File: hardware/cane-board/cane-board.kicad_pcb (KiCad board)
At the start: 2 copper layers, 40 x 100 mm, 99 parts, among them J1 12V battery, J10 Phone power, J11 Firmware, J2 Motor, J3 Kill switch, J4 Talk button, J5 Encoder, J6 I2C, J7 Buzzer motor, J8 Serial, Q1 AO3401A, Q2 AO3401A, Q3 AO3400A, Q4 AO3401A, SW1 Reset, SW2 Boot, SW3 Power, U1 ESP32-S3-WROOM-1-N4, U2 DRV8876PWPR, U3 TPS54302DDCR, U4 AP2112K-3.3, U5 TPS2069CDBVR

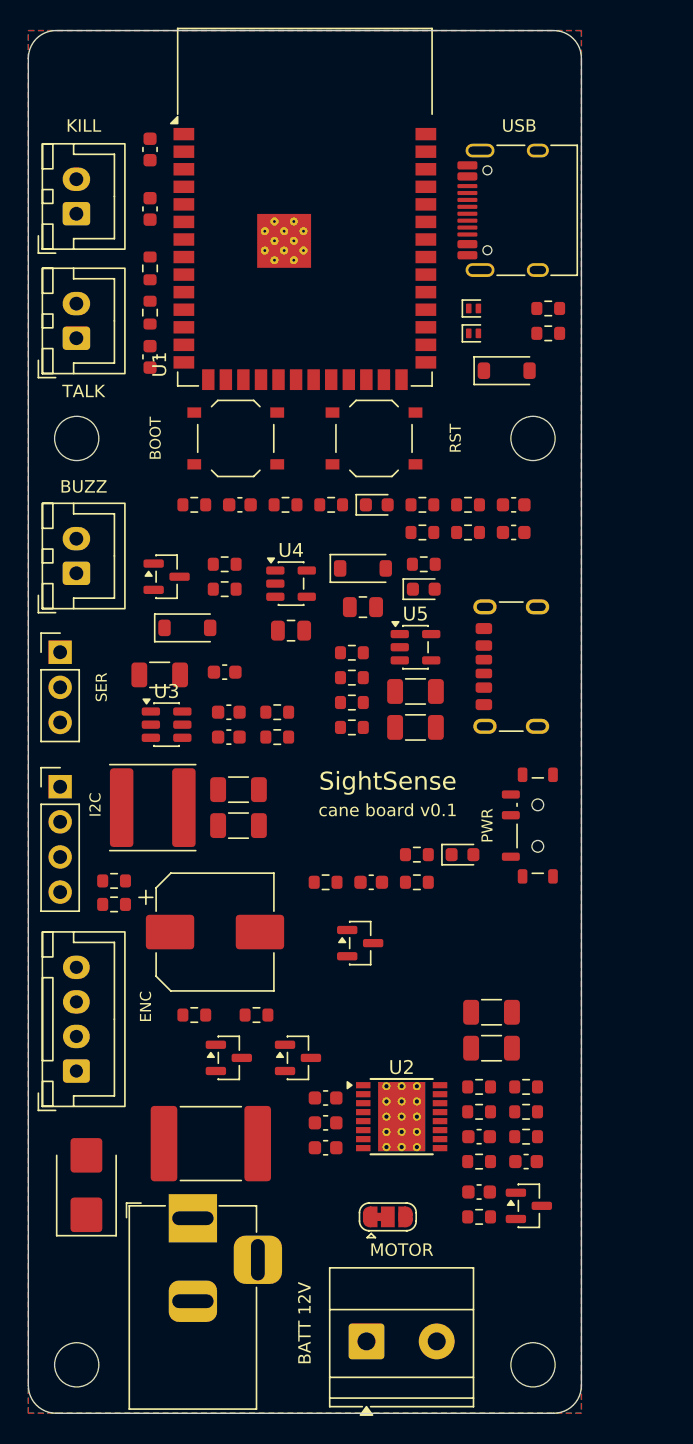
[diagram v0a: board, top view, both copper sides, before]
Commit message: Route the cane board on 4 layers with black mask
make_route.py hands the placed board to Freerouting, widens the motor
supply, pours ground on every layer and stitches it, then runs KiCad's
design rules check: 0 errors, 0 unconnected, matches the schematic.
Adds board rules, mounting screws to the BOM and the 4-layer price.
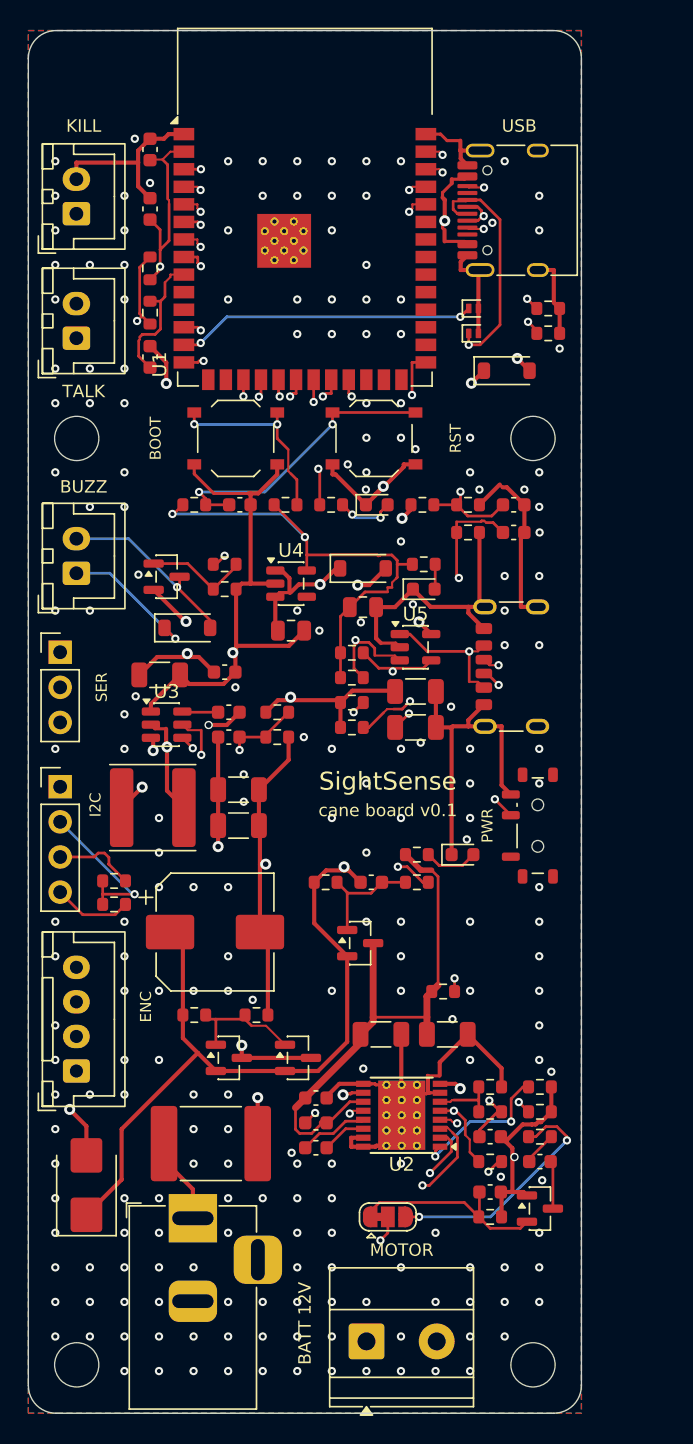
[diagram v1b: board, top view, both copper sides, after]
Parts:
- moved R26 33.2 mm to (30.0, 69.5)
- moved C3 8.16 mm to (25.5, 72.6)
- moved C27 3.35 mm to (30.3, 72.6)
- moved C8 1.00 mm to (37.0, 81.8)
- moved R10 1.00 mm to (37.0, 80.0)
- moved R8 1.00 mm to (37.0, 76.4)
- moved R9 1.00 mm to (37.0, 78.2)
- moved D4 0.82 mm to (37.0, 85.2)
- moved C7 0.80 mm to (33.4, 80.0)
- moved C9 0.80 mm to (33.4, 84.0)
- moved R11 0.80 mm to (33.4, 85.8)
- moved R5 0.80 mm to (33.4, 76.4)
- moved R6 0.80 mm to (33.4, 78.2)
- moved R7 0.80 mm to (33.4, 81.8)
- moved C4 0.70 mm to (20.8, 77.2)
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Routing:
- net GND: track 0.00 -> 210.3 mm, vias 0 -> 218
- net +3V3: track 0.00 -> 164.7 mm, vias 0 -> 6
- net +BATT: track 0.00 -> 107.5 mm, vias 0 -> 4
- net /MOT_EN: track 0.00 -> 102.7 mm, vias 0 -> 3
- net /HBEAT: track 0.00 -> 95.9 mm, vias 0 -> 3
- net /VM_ADC: track 0.00 -> 92.5 mm, vias 0 -> 4
- net /MOT_PH: track 0.00 -> 89.6 mm, vias 0 -> 3
- net /DRV_FLT: track 0.00 -> 88.6 mm, vias 0 -> 4
- net /I_ADC: track 0.00 -> 75.3 mm, vias 0 -> 2
- net +5V: track 0.00 -> 63.6 mm, vias 0 -> 5
- net /KILL_A: track 0.00 -> 63.3 mm, vias 0 -> 2
- net /UART_RX: track 0.00 -> 61.5 mm, vias 0 -> 1
- net /ENC_B: track 0.00 -> 60.2 mm, vias 0 -> 1
- net /ENC_A: track 0.00 -> 52.3 mm, vias 0 -> 1
- net /SDA: track 0.00 -> 50.6 mm, vias 0 -> 1
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- added copper zone on In1.Cu, net GND
- added copper zone on In2.Cu, net GND
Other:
- copper layers 2 -> 4

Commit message: Reroute the cane board at 46 x 100 mm with power on the outer layers
No copper under the ESP32 aerial on any layer; battery, motor and
converter tracks kept to the outer layers; design rules check 0 errors,
0 unconnected, matches the schematic. Adds make_fab.py and the JLCPCB
ordering files. Parts of the VM and MOT_A tracks are still narrow.
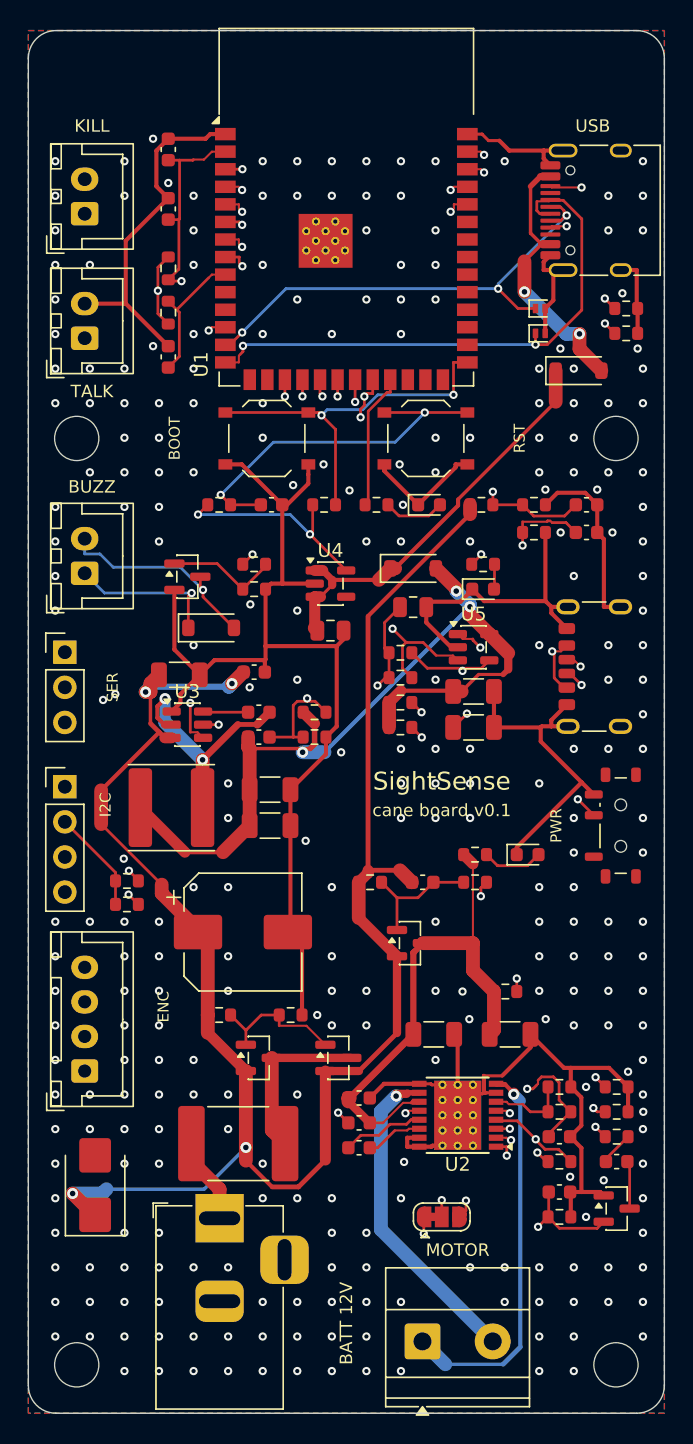
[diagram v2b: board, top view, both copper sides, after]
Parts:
- moved H2 6.00 mm to (42.5, 29.5)
- moved H4 6.00 mm to (42.5, 96.5)
- moved J10 6.00 mm to (42.0, 46.0)
- moved J11 6.00 mm to (41.8, 13.0)
- moved SW3 6.00 mm to (42.8, 57.5)
- moved R19 5.64 mm to (43.2, 20.1)
- moved R20 5.64 mm to (43.2, 21.9)
- moved C8 5.55 mm to (42.5, 81.8)
- moved D4 5.55 mm to (42.5, 85.2)
- moved R10 5.55 mm to (42.5, 80.0)
- moved R8 5.55 mm to (42.5, 76.4)
- moved R9 5.55 mm to (42.5, 78.2)
- moved C22 5.27 mm to (40.4, 34.3)
- moved C23 5.27 mm to (40.4, 36.3)
- moved D6 5.19 mm to (39.8, 24.6)
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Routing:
- net GND: track 210.3 -> 238.4 mm, vias 218 -> 277
- net +BATT: track 107.5 -> 133.3 mm
- net /KILL_A: track 63.3 -> 78.6 mm
- net +3V3: track 164.7 -> 179.4 mm, vias 6 -> 8
- net /UART_RX: track 61.5 -> 50.3 mm
- net /MOT_EN: track 102.7 -> 91.6 mm
- net /BUCK_FB: track 9.93 -> 19.6 mm
- net /VM_ADC: track 92.5 -> 83.6 mm, vias 4 -> 3
- net /ENC_B: track 60.2 -> 52.2 mm, vias 1 -> 3
- net /ENC_A: track 52.3 -> 59.3 mm, vias 1 -> 3
- net /MOT_A: track 23.1 -> 28.4 mm
- net /ESP_EN: track 46.6 -> 51.9 mm
- net /BUCK_SW: track 13.7 -> 18.1 mm
- net /PH_CC1: track 14.3 -> 18.6 mm
- net /DRV_FLT: track 88.6 -> 84.4 mm, vias 4 -> 2
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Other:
- board size 40 x 100 mm -> 46 x 100 mm

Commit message: Cane board: 5 V module, XT30 motor socket, 2.2 A limit, hand-routed power
Replace the TPS54302 converter with a sealed K7805-1000R3 module and
move the power switch to the 3.3 V regulator's enable. Swap the motor
screw terminal for an upright XT30. Raise the current limit to 2.2 A
(R5 1.5k) to match the push the IBT-2 gave.

Draw the battery, motor-supply and motor tracks by hand (0.6-1.0 mm on
the outer layers) before autorouting, turn J2 and C4 round so those
tracks run straight, and tie stranded ground pads to a via. DRC: 0
errors, 0 unconnected. Update the BOM, cost, problems list and fab files.
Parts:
- removed C12: 100nF 50V, Capacitor_SMD:C_0603_1608Metric
- removed C25: 100pF, Capacitor_SMD:C_0603_1608Metric
- removed L1: 10uH 3.2A, Inductor_SMD:L_Changjiang_FNR6045S
- removed R13: 13k, Resistor_SMD:R_0603_1608Metric
- J2: footprint TerminalBlock_Phoenix:TerminalBlock_Phoenix_MKDS-1,5-2-5.08_1x02_P5.08mm_Horizontal -> Connector_AMASS:AMASS_XT30UPB-F_1x02_P5.0mm_Vertical
- R5: value 2.2k -> 1.5k
- U3: value TPS54302DDCR -> K7805-1000R3; footprint Package_TO_SOT_SMD:SOT-23-6 -> Converter_DCDC:Converter_DCDC_RECOM_R-78E-0.5_THT
- moved C13 5.12 mm to (22.6, 54.9)
- moved C14 5.12 mm to (22.6, 57.5)
- moved J2 5.05 mm to (33.5, 94.5), turned to 180 degrees
- moved U3 4.66 mm to (10.5, 54.8)
- moved R12 1.70 mm to (20.7, 47.6)
- turned C4 to 180 degrees
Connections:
- R12 pad 1: +5V -> /VSYS
- R12 pad 2: /BUCK_FB -> /LDO_EN
- SW3 pad 2: /BUCK_EN -> /LDO_EN
- U3 pad 1: GND -> +BATT
- U3 pad 2: /BUCK_SW -> GND
- U3 pad 3: +BATT -> +5V
- U4 pad 3: /VSYS -> /LDO_EN
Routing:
- net /LDO_EN: track 0.00 -> 37.8 mm, vias 0 -> 2
- net /BUCK_EN: track 31.0 -> 0.00 mm, vias 2 -> 0
- net GND: track 238.4 -> 209.5 mm, vias 277 -> 263
- net /UART_TX: track 48.8 -> 76.6 mm
- net /BUCK_FB: track 19.6 -> 0.00 mm, vias 2 -> 0
- net /BUCK_SW: track 18.1 -> 0.00 mm, vias 2 -> 0
- net +BATT: track 133.3 -> 116.3 mm
- net /KILL_A: track 78.6 -> 66.2 mm
- net +5V: track 61.6 -> 50.2 mm, vias 3 -> 1
- net /DRV_FLT: track 84.4 -> 92.8 mm, vias 2 -> 3
- net /ENC_B: track 52.2 -> 59.8 mm, vias 3 -> 2
- net /MOT_A: track 28.4 -> 21.0 mm
- net +3V3: track 179.4 -> 186.4 mm
- net /MOT_EN: track 91.6 -> 97.9 mm
- net /ENC_A: track 59.3 -> 53.3 mm, vias 3 -> 2
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
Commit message: Cane board: cooler kill-switch FET, keep braking, battery plug notes
R2 and R3 go from 47k and 100k to 10k and 13k, so Q2's gate gets 0.43
of the battery instead of a third: 3.9 V from a flat 9 V pack (about
0.3 W at the 2.2 A limit instead of 0.4 W) and 10.6 V at the TVS
clamp, still under its 12 V limit. The kill switch now carries about
0.5 mA and cuts the motor supply in about 2 ms. Values only: the routed
board, Gerbers and placement file are unchanged; DRC 0 errors, 0
unconnected, schematic and board values match.

PMODE stays on ground (PH/EN mode, so a commanded stop brakes). The
worm gear holds the wheel either way and a dropped link still sleeps
the driver, which coasts as the IBT-2 did; firmware can coast for FREE
by stopping the heartbeat. Recorded in the README and as decided in
POTENTIAL_PROBLEMS.md, with how to check the battery plug.

The schematic picture is redrawn from the current PDF; it still showed
the old TPS54302 converter.
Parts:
- R2: value 47k -> 10k
- R3: value 100k -> 13k
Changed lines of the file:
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@@
 			)
 		)
-		(property "Value" "47k"
+		(property "Value" "10k"
 			(at 0 1.43 0)
 			(layer "F.Fab")
@@
 			)
 		)
-		(property "Value" "100k"
+		(property "Value" "13k"
 			(at 0 1.43 0)
 			(layer "F.Fab")

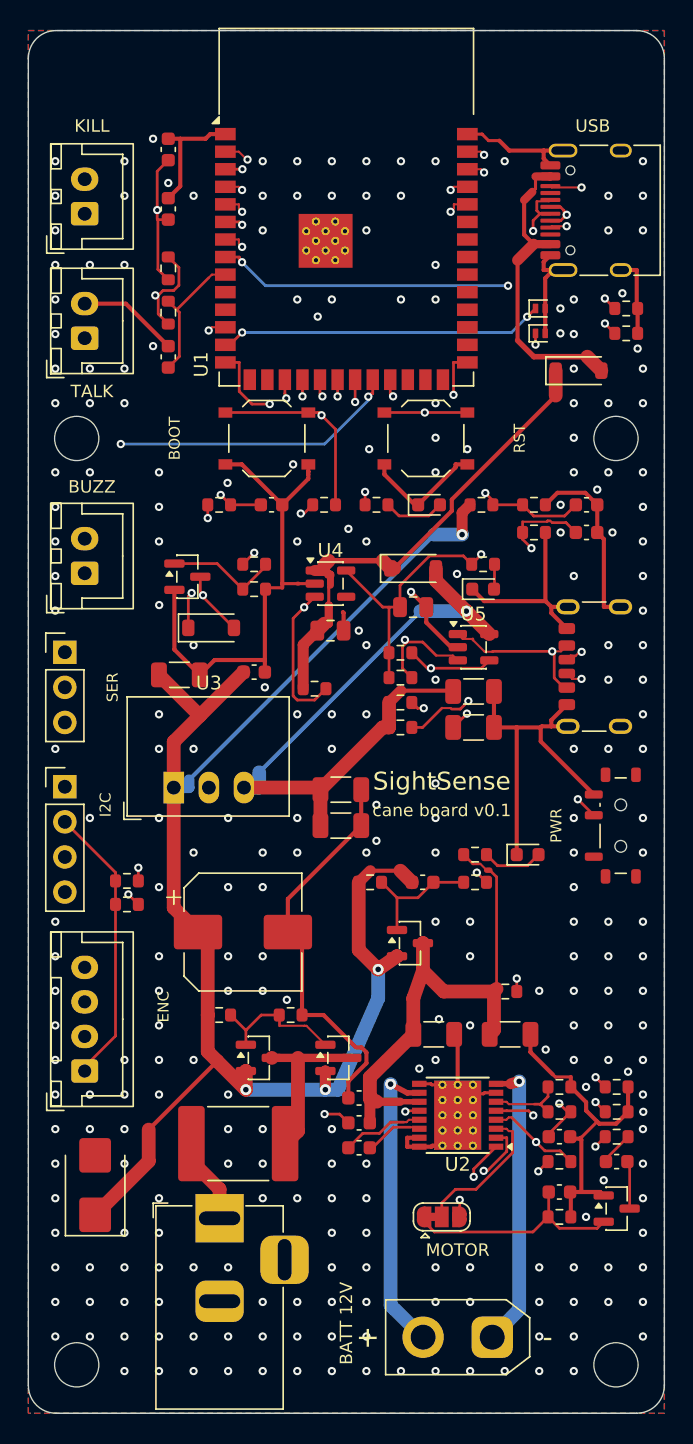
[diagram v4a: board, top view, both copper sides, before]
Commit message: Cane board: pre-order checks against JLCPCB, larger print, stock and pin-1 notes
Checked before ordering, all recorded in POTENTIAL_PROBLEMS.md:

- The board's rules and smallest features against JLCPCB's 4-layer
  limits: tracks 0.15 mm, gaps 0.15, vias 0.6/0.3, holes 0.3, copper
  0.5 from the edge, mask dams 0.2 mm at the tightest pins (black
  needs 0.13). All inside.
- The placement file, the BOM and the board list the same 82 fitted
  parts and none of the 8 unfitted ones.
- Stock on LCSC for the six parts that matter most: all in stock; the
  processor module is the thinnest line at 2,222. The 220 uF can is
  8 mm across, as the footprint expects.
- Where pin 1 sits on every keyed part, for the placement preview.

The printed labels are raised to JLCPCB's 1.0 mm / 0.15 mm minimum,
the version label is shortened to clear two capacitor pads, and U3's
print is hidden (the module carries its own). Copper is unchanged:
the copper and drill Gerbers differ only by date. DRC 0 errors, 0
unconnected, 3 warnings. make_pcb.py carries the same print sizes.
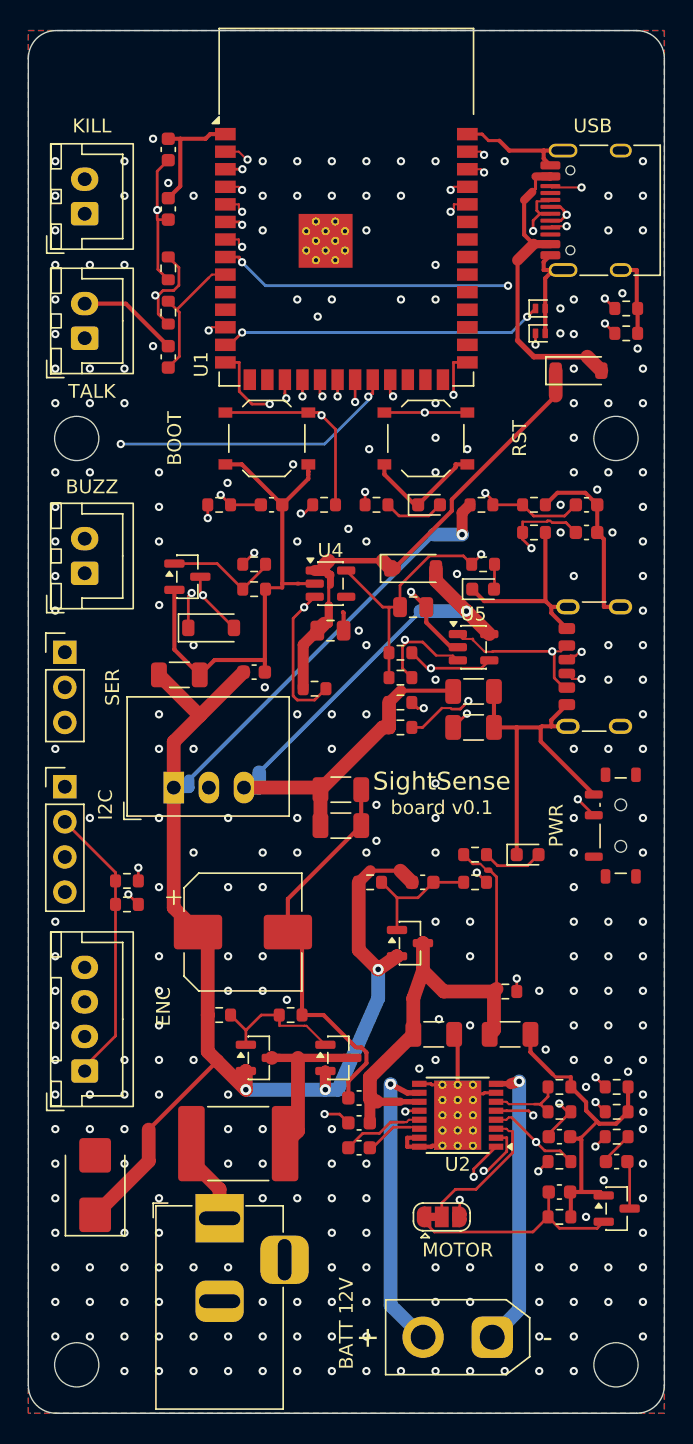
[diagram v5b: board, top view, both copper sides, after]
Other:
- board text added: "board v0.1"
- board text removed: "cane board v0.1"
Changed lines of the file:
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@@
 			(at 2.54 -7.56 0)
 			(layer "F.SilkS")
+			(hide yes)
 			(effects
 				(font
@@
 		(layer "Edge.Cuts")
 	)
-	(gr_text "I2C"
-		(at 5.58 56 90)
+	(gr_text "KILL"
+		(at 4.6 6.9 0)
 		(layer "F.SilkS")
 		(effects
 			(font
-				(size 0.8 0.8)
-				(thickness 0.12)
+				(size 1 1)
+				(thickness 0.15)
 			)
 		)
 	)
-	(gr_text "SER"
-		(at 6.09 47.5 90)
+	(gr_text "TALK"
+		(at 4.6 26.1 0)
 		(layer "F.SilkS")
 		(effects
 			(font
-				(size 0.8 0.8)
-				(thickness 0.12)
+				(size 1 1)
+				(thickness 0.15)
 			)
 		)
 	)
-	(gr_text "ENC"
-		(at 9.77 70.6 90)
+	(gr_text "BUZZ"
+		(at 4.6 33 0)
 		(layer "F.SilkS")
 		(effects
 			(font
-				(size 0.8 0.8)
-				(thickness 0.12)
+				(size 1 1)
+				(thickness 0.15)
 			)
 		)
 	)
-	(gr_text "BOOT"
-		(at 10.58 29.5 90)
+	(gr_text "board v0.1"
+		(at 29.9 56.2 0)
 		(layer "F.SilkS")
 		(effects
 			(font
-				(size 0.8 0.8)
-				(thickness 0.12)
+				(size 1 1)
+				(thickness 0.15)
 			)
 		)
 	)
-	(gr_text "RST"
-		(at 35.53 29.5 90)
+	(gr_text "MOTOR"
+		(at 31.05 88.2 0)
 		(layer "F.SilkS")
 		(effects
 			(font
-				(size 0.8 0.8)
-				(thickness 0.12)
+				(size 1 1)
+				(thickness 0.15)
 			)
 		)
 	)
-	(gr_text "PWR"
-		(at 38.18 57.5 90)
+	(gr_text "USB"
+		(at 40.82 6.9 0)
 		(layer "F.SilkS")
 		(effects
 			(font
-				(size 0.8 0.8)
-				(thickness 0.12)
+				(size 1 1)
+				(thickness 0.15)
 			)
 		)
 	)
-	(gr_text "KILL"
-		(at 4.6 6.9 0)
+	(gr_text "I2C"
+		(at 5.58 56 90)
 		(layer "F.SilkS")
 		(effects
 			(font
-				(size 0.9 0.9)
-				(thickness 0.135)
+				(size 1 1)
+				(thickness 0.15)
 			)
 		)
 	)
-	(gr_text "TALK"
-		(at 4.6 26.1 0)
+	(gr_text "SER"
+		(at 6.09 47.5 90)
 		(layer "F.SilkS")
 		(effects
 			(font
-				(size 0.9 0.9)
-				(thickness 0.135)
+				(size 1 1)
+				(thickness 0.15)
 			)
 		)
 	)
-	(gr_text "BUZZ"
-		(at 4.6 33 0)
+	(gr_text "ENC"
+		(at 9.77 70.6 90)
 		(layer "F.SilkS")
 		(effects
 			(font
-				(size 0.9 0.9)
-				(thickness 0.135)
+				(size 1 1)
+				(thickness 0.15)
 			)
 		)
 	)
-	(gr_text "cane board v0.1"
-		(at 29.9 56.4 0)
+	(gr_text "BOOT"
+		(at 10.58 29.5 90)
 		(layer "F.SilkS")
 		(effects
 			(font
-				(size 0.9 0.9)
-				(thickness 0.135)
+				(size 1 1)
+				(thickness 0.15)
 			)
 		)
 	)
-	(gr_text "MOTOR"
-		(at 31.05 88.2 0)
+	(gr_text "BATT 12V"
+		(at 23 93.5 90)
 		(layer "F.SilkS")
 		(effects
 			(font
-				(size 0.9 0.9)
-				(thickness 0.135)
+				(size 1 1)
+				(thickness 0.15)
 			)
 		)
 	)
-	(gr_text "USB"
-		(at 40.82 6.9 0)
+	(gr_text "RST"
+		(at 35.53 29.5 90)
 		(layer "F.SilkS")
 		(effects
 			(font
-				(size 0.9 0.9)
-				(thickness 0.135)
+				(size 1 1)
+				(thickness 0.15)
 			)
 		)
 	)
-	(gr_text "BATT 12V"
-		(at 23 93.5 90)
+	(gr_text "PWR"
+		(at 38.18 57.5 90)
 		(layer "F.SilkS")
 		(effects
 			(font
-				(size 0.9 0.9)
-				(thickness 0.135)
+				(size 1 1)
+				(thickness 0.15)
 			)
 		)
